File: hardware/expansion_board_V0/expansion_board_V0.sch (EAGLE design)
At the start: 499 parts, among them CON1 ELEC, CON10 M5, CON11 M2, CON12 M4, CON13 M1, CON14 ESC0, CON15 CON10_2_2.54, CON16 CON10_2_2.54, CON17 ESC1, CON18 UART0, CON19 QEI1, CON2 SERVO, CON20 AN0, CON21 S0, CON22 IO0, CON23 AN1, CON24 S1, CON25 IO1, CON26 UART1, CON27 QEI0, CON28 AN2, CON29 S2, CON3 LIPO_MOT, CON30 IO2, CON31 TELEM, CON32 QEI3, CON33 AN3, CON34 S3, CON35 IO3, CON36 BALISE, CON37 AN4, CON38 S4, CON39 IO4, CON4 LIPO_MOT, CON40 SPI0, CON41 QEI2, CON42 AN5, CON43 S5, CON44 IO5, CON45 SPI1, CON46 AN6, CON47 S6, CON48 IO6, CON49 I2C0, CON5 LIPO_MOT, CON50 AN7, CON51 S7, CON52 IO7, CON53 I2C1, CON54 USB2, CON55 USB3, CON56 USBfpga, CON57 FPGA_GPIO0, CON58 FPGA_GPIO1, CON59 FPGA_LTC, CON6 LIPO_MOT, CON60 USB3, CON61 CON5_2.54S, CON62 CON5_2.54S, CON63 CON5_2.54S, CON64 CON5_2.54S, CON7 FPGApower, CON8 M0, CON9 M3, IC1 ADS1258, IC2 ADS1278, IC3 REF5030I, IC4 REF5025I, J1 NC, J10 0, J11 0, J12 0, J13 0, J14 0, J15 0, J16 0, J17 0, J18 0, J19 0, J2 nc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

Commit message: PCB envoyé chez eurocircuit
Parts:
- added J50, J51: 0, iocene:JUMP_402
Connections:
- new net N$98: J50.2, J51.1, U37.FSYNC
- net GND: now also J50.1
- net IMU_FSYNC: now also J51.2, U29./RESET; no longer U37.FSYNC
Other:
- moved on the sheet: C159, C160, C161, C162, C163, C164, C165, C166, C167, C168, C169, C170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

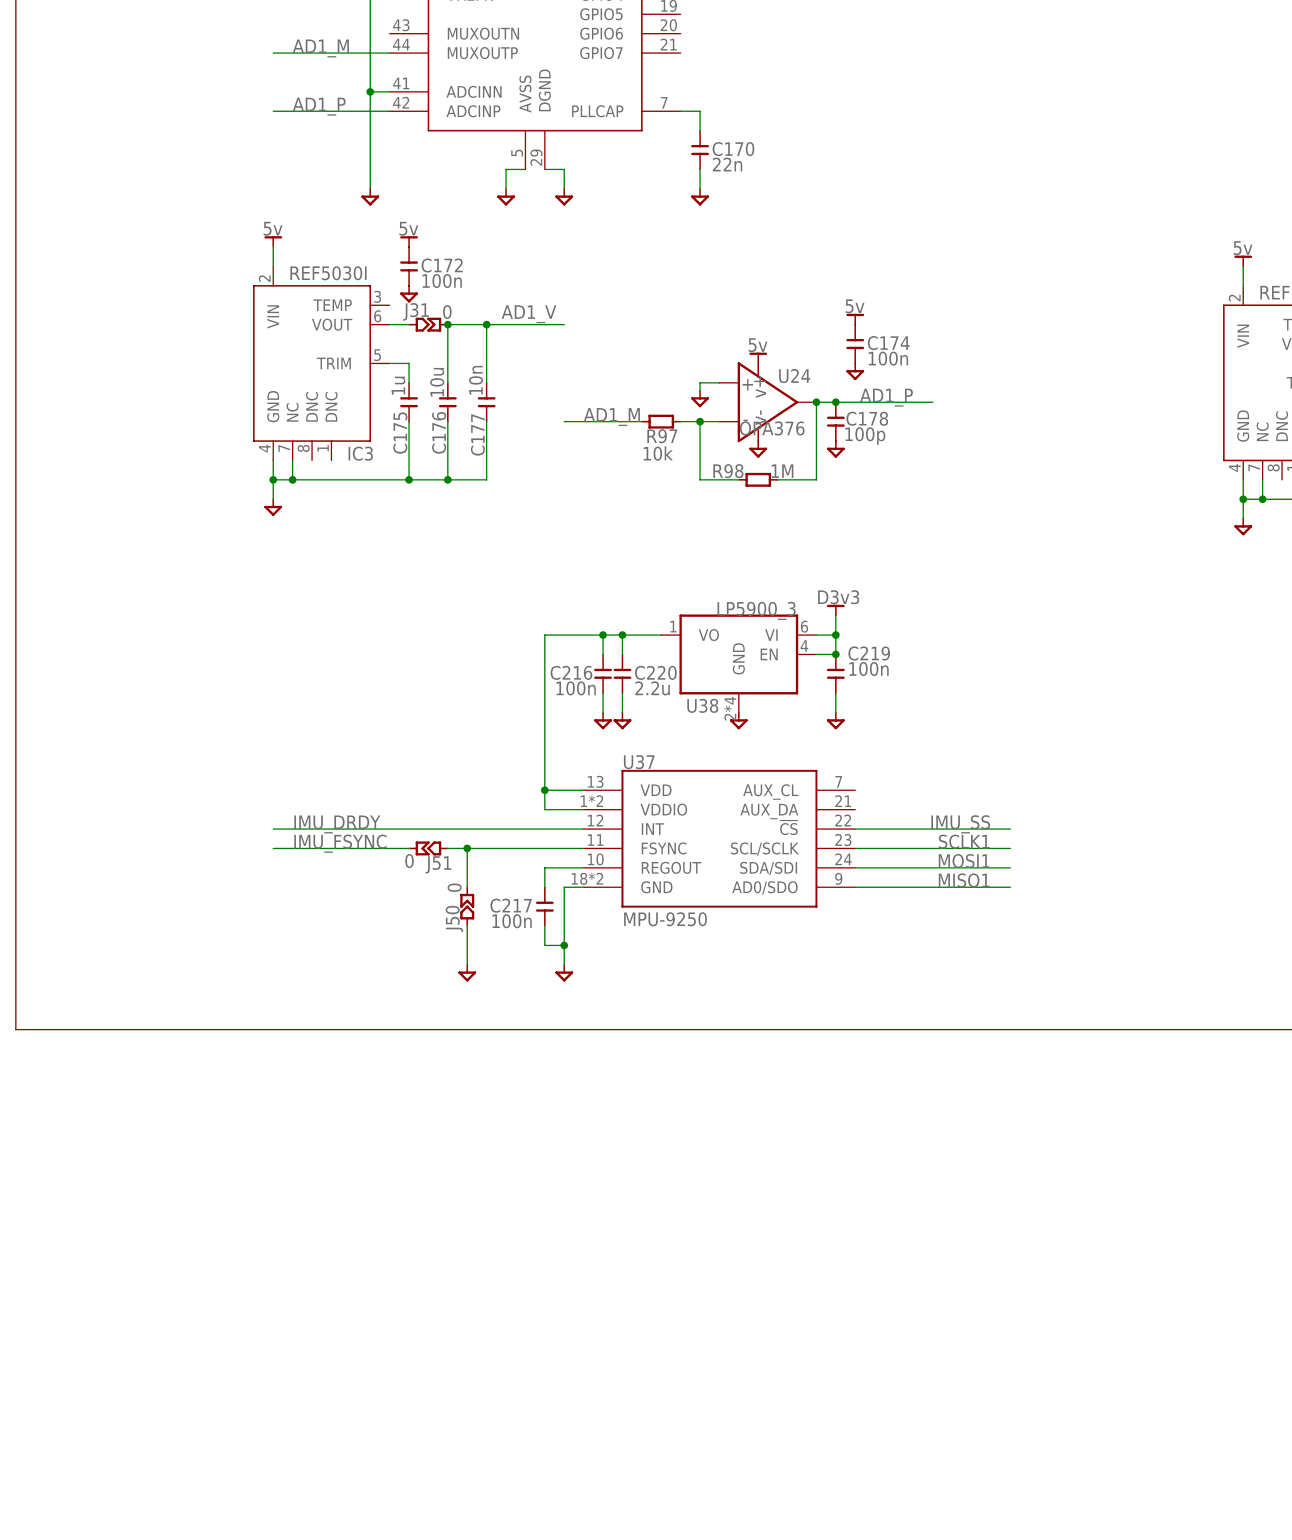
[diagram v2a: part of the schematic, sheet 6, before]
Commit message: Update schematics with new library
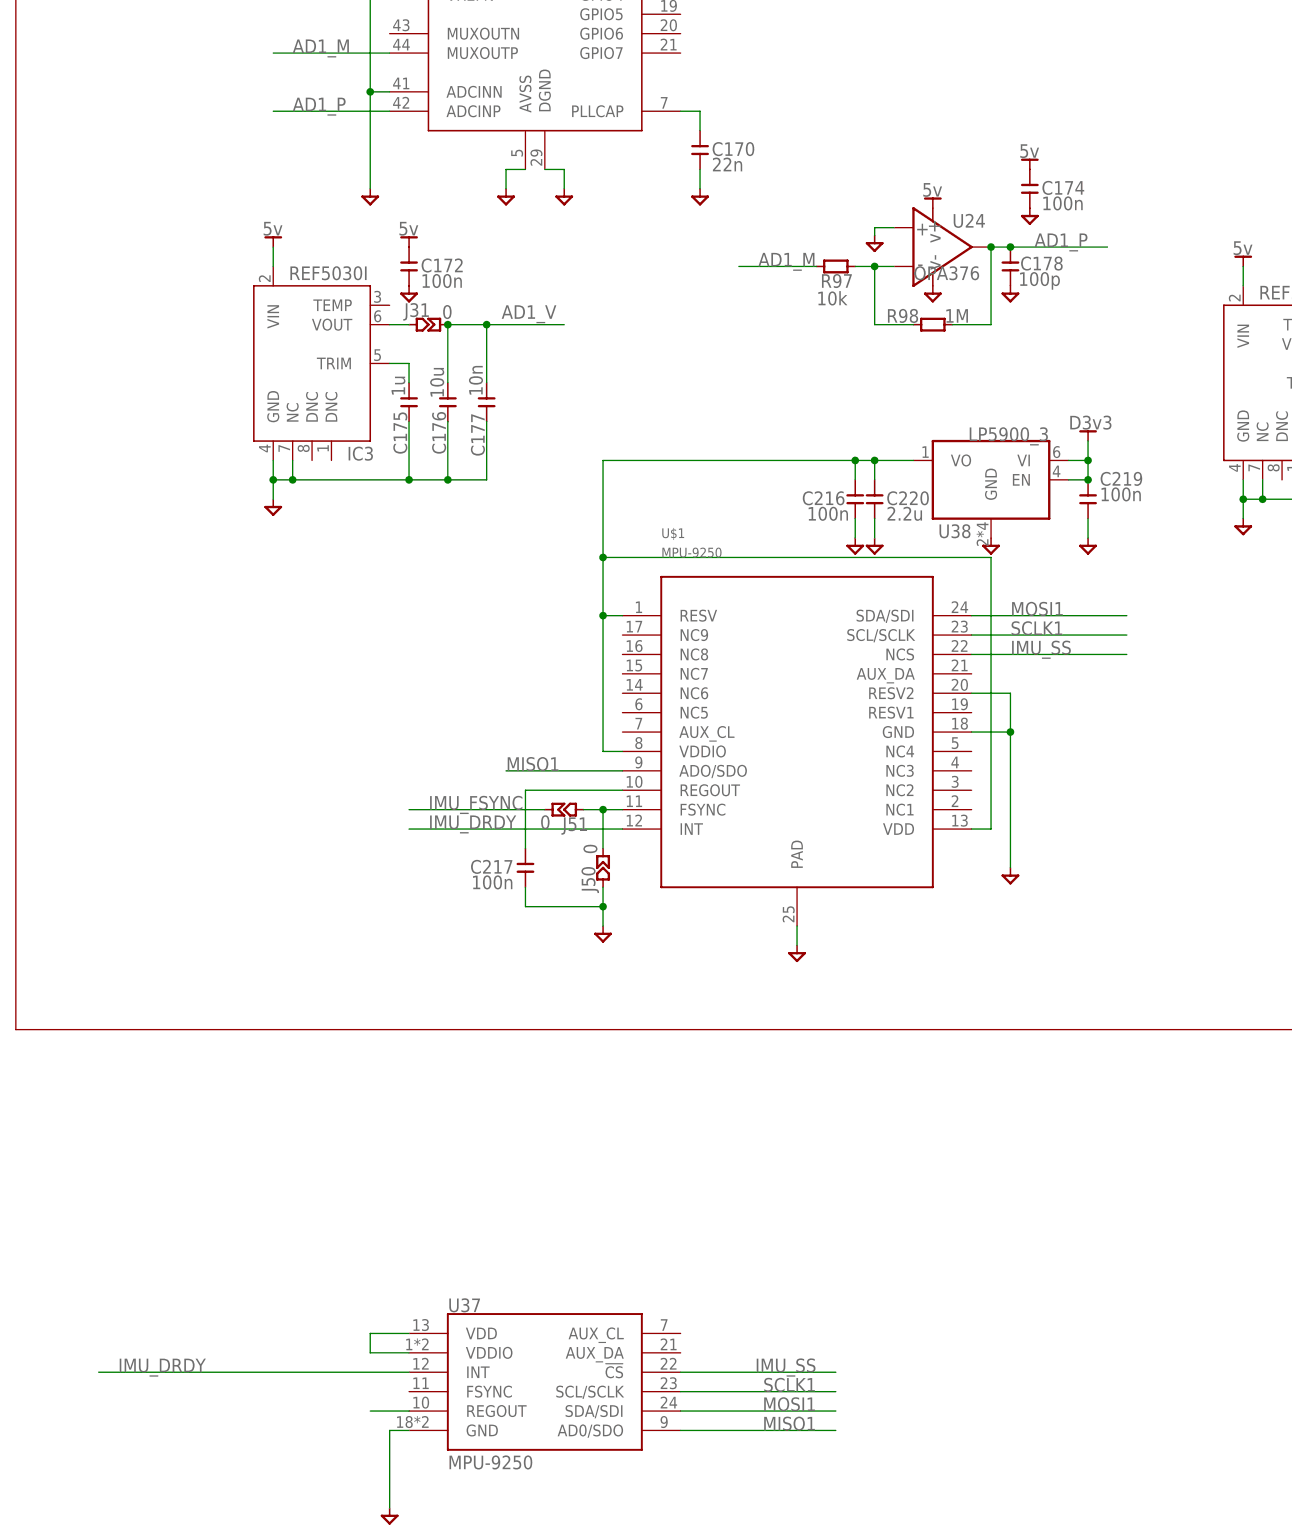
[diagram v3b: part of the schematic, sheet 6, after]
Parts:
- added U$1: MPU-9250, invensense:MPU-9250
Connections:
- new net N$107: C217.P$2, U$1.REGOUT
- new net N$141: U37.VDD, U37.VDDIO
- net GND: now also U$1.GND, U$1.PAD, U$1.RESV2
- net IMU_DRDY: now also U$1.INT
- net IMU_SS: now also U$1.NCS
- net MISO1: now also U$1.ADO/SDO
- net MOSI1: now also U$1.SDA/SDI
- net N$74: now also U$1.RESV, U$1.VDD, U$1.VDDIO; no longer U37.VDD, U37.VDDIO
- net N$98: now also U$1.FSYNC; no longer U37.FSYNC
- net REGOUT1: no longer C217.P$2
- net SCLK1: now also U$1.SCL/SCLK
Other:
- moved on the sheet: C174, C178, C216, C217, C219, C220, J50, J51, R97, R98, U24, U37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

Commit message: IMU footprint ok Elec posté sur Eurocircuit
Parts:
- removed U$1: MPU-9250, invensense:MPU-9250
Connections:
- removed net N$107: C217.P$2, U$1.REGOUT
- removed net N$141: U37.VDD, U37.VDDIO
- net GND: no longer U$1.GND, U$1.PAD, U$1.RESV2
- net IMU_DRDY: no longer U$1.INT
- net IMU_SS: no longer U$1.NCS
- net MISO1: no longer U$1.ADO/SDO
- net MOSI1: no longer U$1.SDA/SDI
- net N$74: now also U37.VDD, U37.VDDIO; no longer U$1.RESV, U$1.VDD, U$1.VDDIO
- net N$98: now also U37.FSYNC; no longer U$1.FSYNC
- net REGOUT1: now also C217.P$2
- net SCLK1: no longer U$1.SCL/SCLK
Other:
- moved on the sheet: C174, C178, C216, C217, C219, C220, J50, J51, R97, R98, U24, U37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

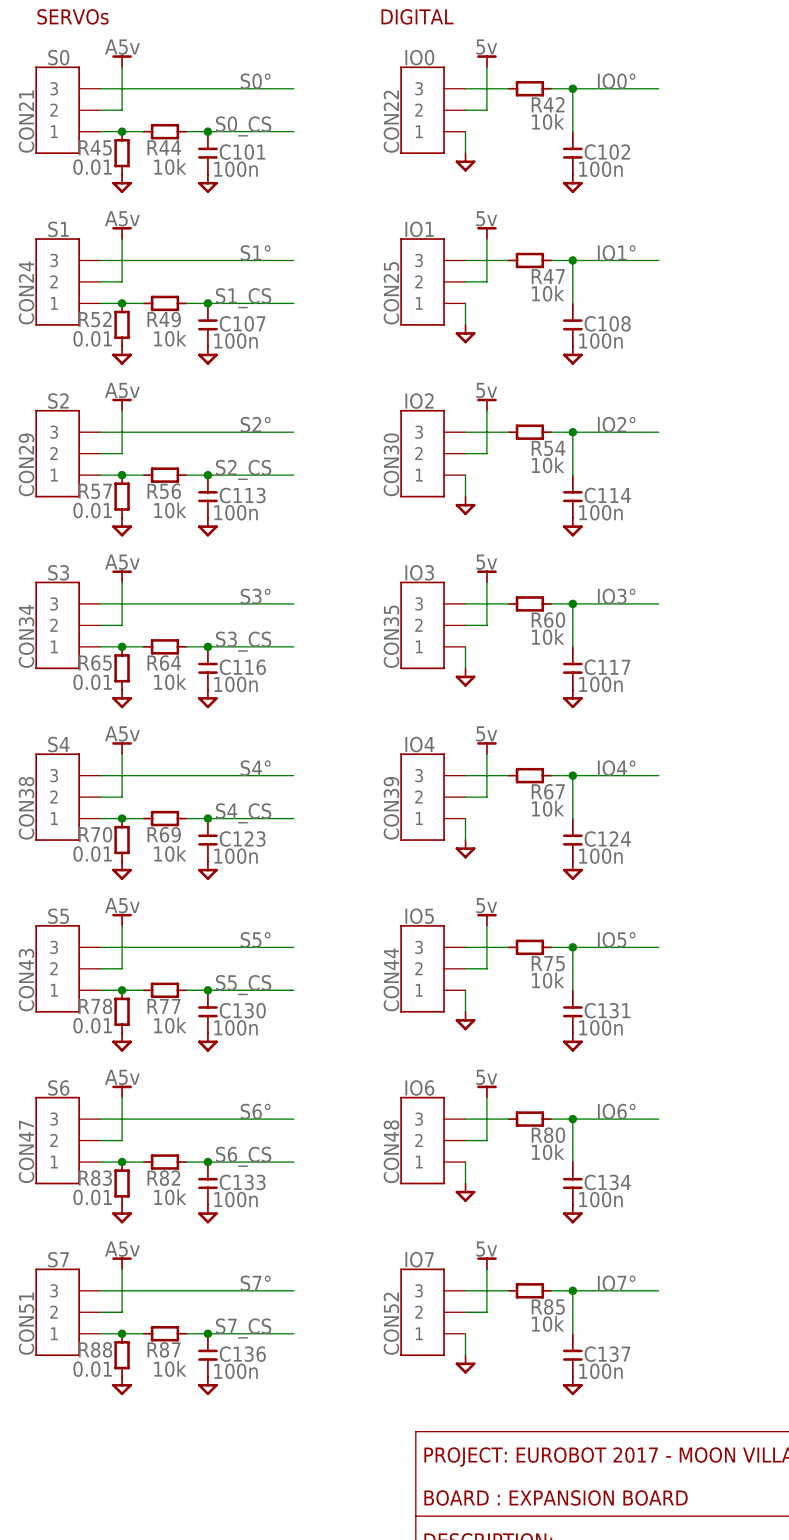
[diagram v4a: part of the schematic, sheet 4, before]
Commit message: Ajout de commentaires bug carte électronique sur le schéma
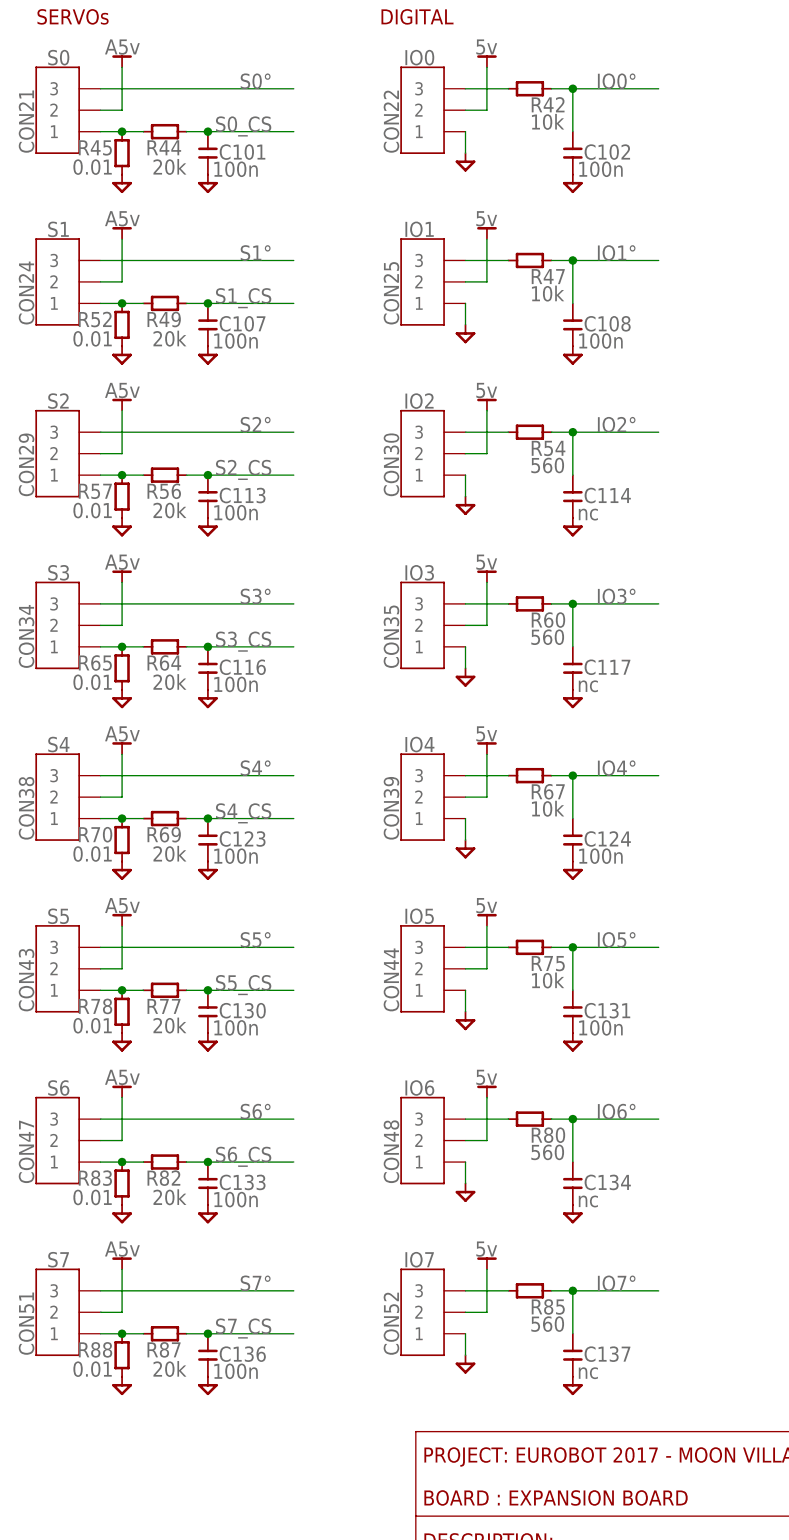
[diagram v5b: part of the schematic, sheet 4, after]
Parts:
- C114, C117, C134, C137: value 100n -> nc
- C168, C169: value 22n -> 8p
- C19: value nc -> 22n
- C23: value nc -> 1n
- R100, R101, R102, R103, R104, R105, R106, R99: value 10k -> 50k
- R44, R49, R56, R64, R69, R77, R82, R87: value 10k -> 20k
- R54, R60, R80, R85: value 10k -> 560
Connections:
- net M4_CS renamed M5_CS
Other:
- note added: "Delete power pad on DRV8402"
- note added: "FOOTPRINT error, manque pin 1?"
- note added: "Footprint reversed and pitch error on INA240"
- note added: "Footprint trop large"
- note added: "Manque des résistances de pull up"

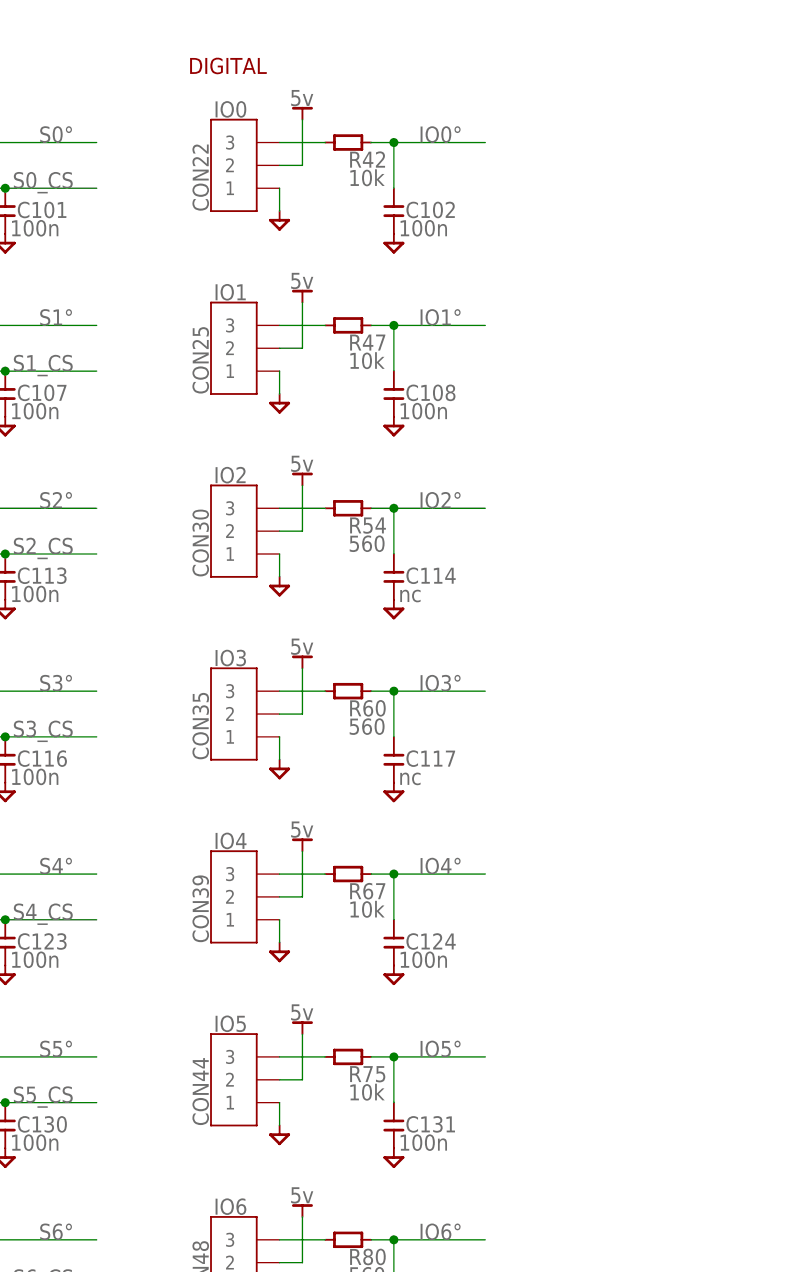
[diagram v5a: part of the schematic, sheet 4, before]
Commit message: Add datasheet capteur couleur
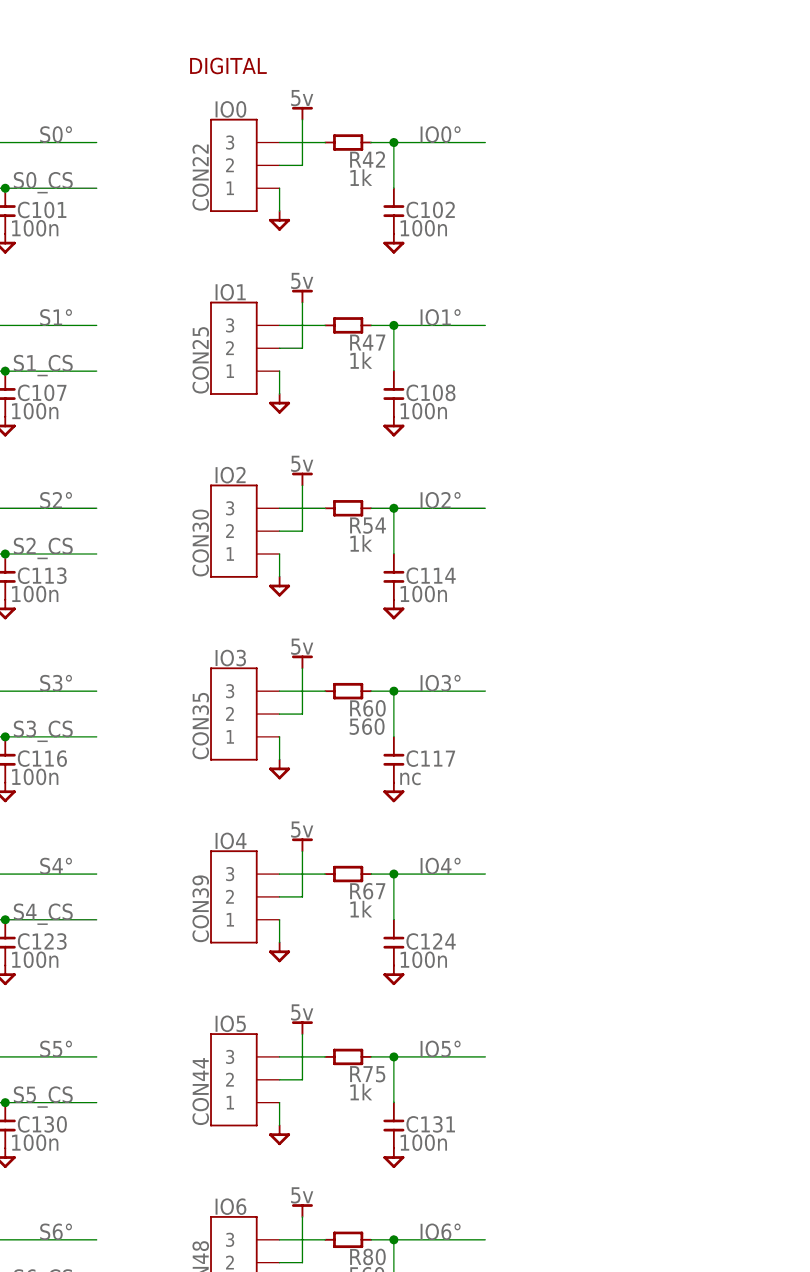
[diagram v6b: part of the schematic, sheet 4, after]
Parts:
- C114: value nc -> 100n
- R42, R47, R67, R75: value 10k -> 1k
- R54: value 560 -> 1k
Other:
- note added: "Add pulldown 1k on output (bitstream loading)"
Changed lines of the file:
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@@
 <part name="C102" library="iocene" deviceset="C" device="_402" value="100n"/>
 <part name="GND100" library="iocene" deviceset="GND" device=""/>
-<part name="R42" library="iocene" deviceset="R" device="_402" value="10k"/>
+<part name="R42" library="iocene" deviceset="R" device="_402" value="1k"/>
 <part name="5V22" library="iocene" deviceset="5V" device=""/>
 <part name="CON25" library="iocene" deviceset="CON3" device="_SMT" value="IO1"/>
@@
 <part name="C108" library="iocene" deviceset="C" device="_402" value="100n"/>
 <part name="GND108" library="iocene" deviceset="GND" device=""/>
-<part name="R47" library="iocene" deviceset="R" device="_402" value="10k"/>
+<part name="R47" library="iocene" deviceset="R" device="_402" value="1k"/>
 <part name="5V25" library="iocene" deviceset="5V" device=""/>
 <part name="CON30" library="iocene" deviceset="CON3" device="_SMT" value="IO2"/>
 <part name="GND120" library="iocene" deviceset="GND" device=""/>
-<part name="C114" library="iocene" deviceset="C" device="_402" value="nc"/>
+<part name="C114" library="iocene" deviceset="C" device="_402" value="100n"/>
 <part name="GND116" library="iocene" deviceset="GND" device=""/>
-<part name="R54" library="iocene" deviceset="R" device="_402" value="560"/>
+<part name="R54" library="iocene" deviceset="R" device="_402" value="1k"/>
 <part name="5V28" library="iocene" deviceset="5V" device=""/>
 <part name="CON35" library="iocene" deviceset="CON3" device="_SMT" value="IO3"/>
@@
 <part name="C124" library="iocene" deviceset="C" device="_402" value="100n"/>
 <part name="GND131" library="iocene" deviceset="GND" device=""/>
-<part name="R67" library="iocene" deviceset="R" device="_402" value="10k"/>
+<part name="R67" library="iocene" deviceset="R" device="_402" value="1k"/>
 <part name="5V34" library="iocene" deviceset="5V" device=""/>
 <part name="CON44" library="iocene" deviceset="CON3" device="_SMT" value="IO5"/>
@@
 <part name="C131" library="iocene" deviceset="C" device="_402" value="100n"/>
 <part name="GND139" library="iocene" deviceset="GND" device=""/>
-<part name="R75" library="iocene" deviceset="R" device="_402" value="10k"/>
+<part name="R75" library="iocene" deviceset="R" device="_402" value="1k"/>
 <part name="5V38" library="iocene" deviceset="5V" device=""/>
 <part name="CON48" library="iocene" deviceset="CON3" device="_SMT" value="IO6"/>
@@
 <text x="93.98" y="40.64" size="1.778" layer="94">LTC connector</text>
 <text x="58.42" y="12.7" size="1.778" layer="98" rot="R90">Analog pin, do not use</text>
+<text x="104.14" y="215.9" size="1.778" layer="98">Add pulldown 1k on output  (bitstream loading)</text>
 </plain>
 <instances>
